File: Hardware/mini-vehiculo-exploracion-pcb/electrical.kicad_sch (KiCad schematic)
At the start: 0 parts

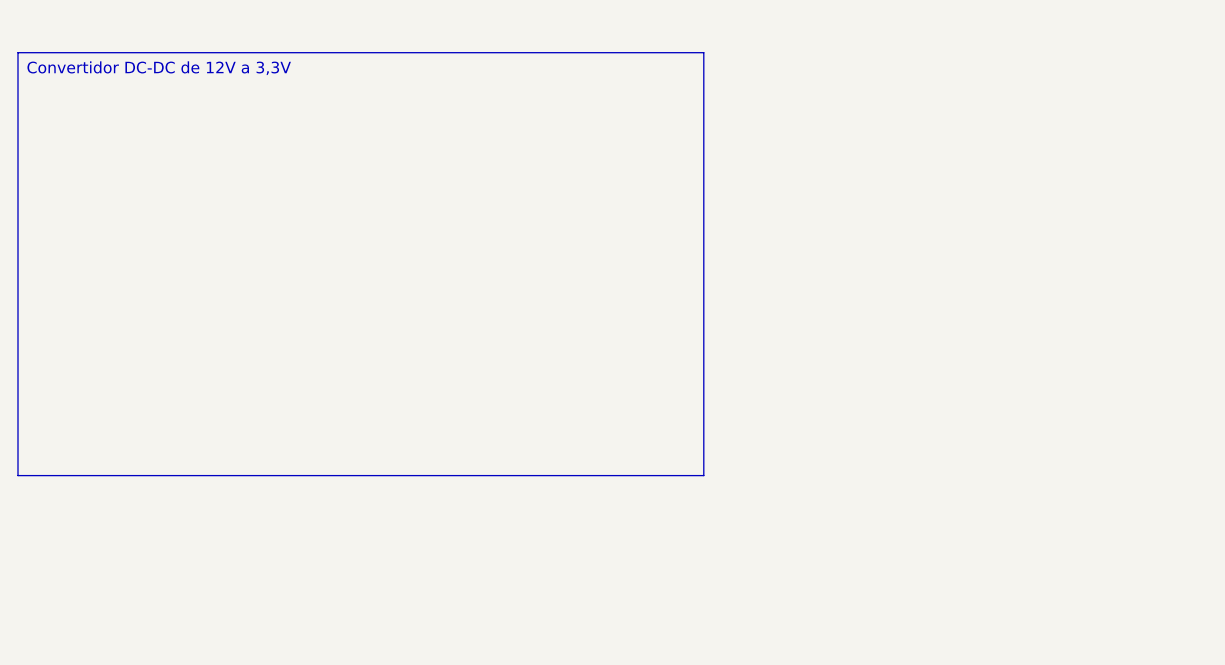
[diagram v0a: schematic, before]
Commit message: implementacion buck 3,3V
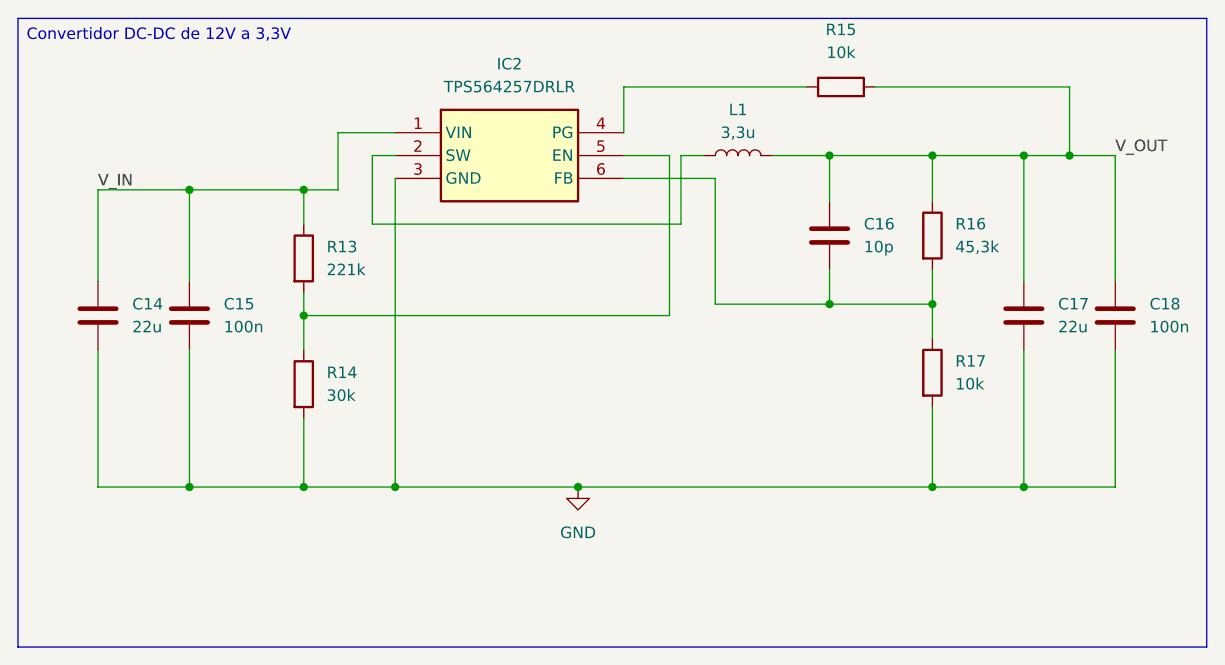
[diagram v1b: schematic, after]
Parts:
- added C14, C17: 22u, symbol Device:C
- added C15, C18: 100n, symbol Device:C
- added C16: 10p, symbol Device:C
- added IC2: TPS564257DRLR, SOTFL50P160X60-6N, symbol SamacSys_Parts:TPS564257DRLR
- added L1: 3,3u, symbol Device:L
- added R13: 221k, symbol Device:R
- added R14: 30k, symbol Device:R
- added R15, R17: 10k, symbol Device:R
- added R16: 45,3k, symbol Device:R
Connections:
- new net: C16.2, IC2.6 (FB), R16.2, R17.1
- new net: IC2.2 (SW), L1.1
- new net: IC2.5 (EN), R13.2, R14.1
- new net: IC2.4 (PG), R15.1
- new net GND: C14.2, C15.2, C17.2, C18.2, IC2.3 (GND), R14.2, R17.2
- new net V_IN: C14.1, C15.1, IC2.1 (VIN), R13.1
- new net V_OUT: C16.1, C17.1, C18.1, L1.2, R15.2, R16.1

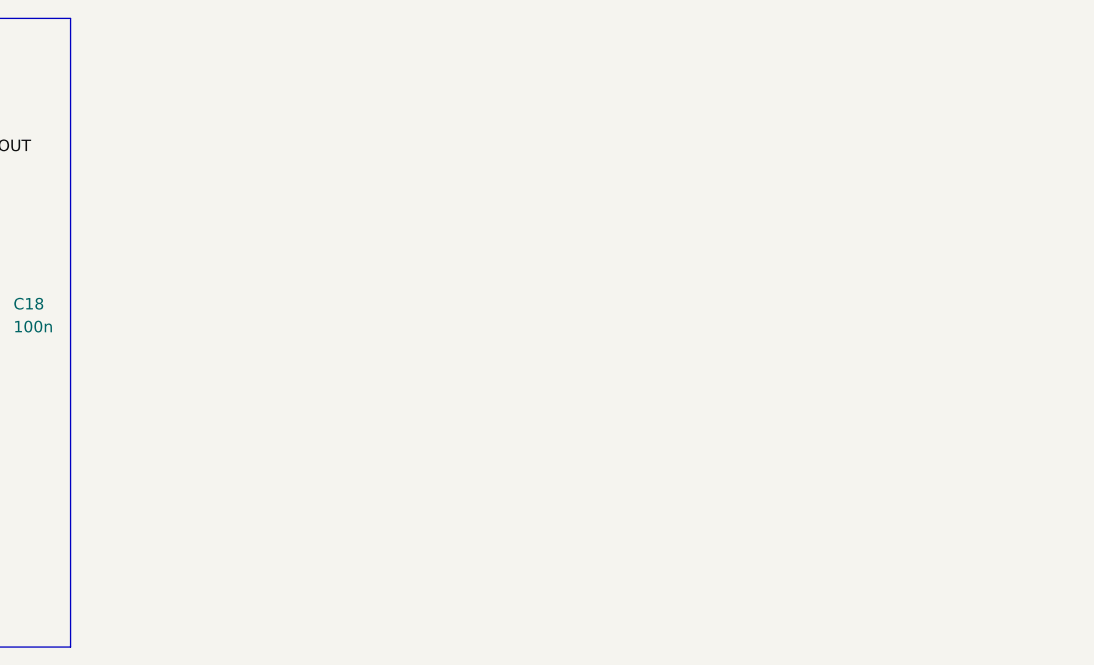
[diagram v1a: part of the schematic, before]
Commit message: LDO 5V a 3,3V
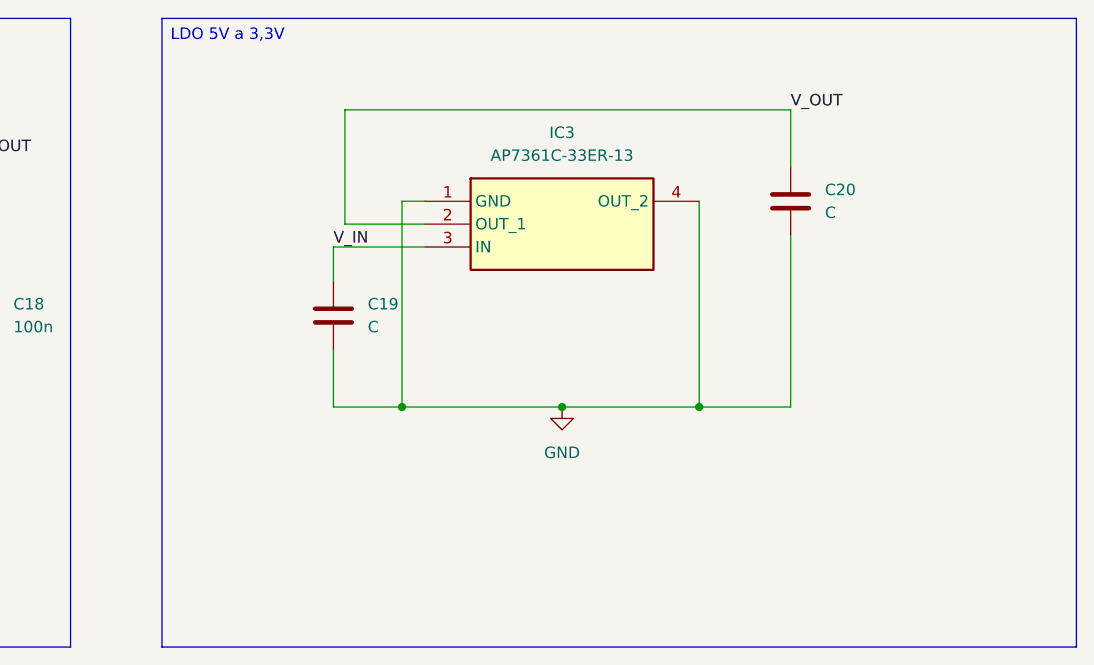
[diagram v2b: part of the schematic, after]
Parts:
- added C19, C20: C, symbol Device:C
- added IC3: AP7361C-33ER-13, SOT230P700X180-4N, symbol SamacSys_Parts:AP7361C-33ER-13
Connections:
- net GND: now also C19.2, C20.2, IC3.1 (GND), IC3.4 (OUT_2)
- net V_IN: now also C19.1, IC3.3 (IN)
- net V_OUT: now also C20.1, IC3.2 (OUT_1)

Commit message: Carga de librerias
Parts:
- added C21: 47nF, symbol Device:C
- added D3: PTVS13VP1UTP-QX, SODFL4725X110N, symbol PTVS13VP1UTP-QX:PTVS13VP1UTP-QX
- added F2: SMD200F_24-2920-2, SMD200F2429202, symbol SMD200F_24-2920-2:SMD200F_24-2920-2
- added IC4: NCV68061SNAIT1G, SOT95P275X110-6N, symbol NCV68061SNAIT1G:NCV68061SNAIT1G
- added Q1: NVMFS5C442NLAFT1G-YE, NVMFS5C430NAFT1GYE, symbol NVMFS5C442NLAFT1G-YE:NVMFS5C442NLAFT1G-YE
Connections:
- net GND: now also C21.2, D3.2 (A), IC4.2 (GND), IC4.4 (D)
- new net: D3.1 (K), F2.1
- new net: F2.2, IC4.3 (EN)
- new net: C21.1, IC4.6 (S)

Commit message: edicion parcial proteccion entrada
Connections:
- net at Q1.4 (G): now also IC4.5 (G)
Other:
- moved on the sheet: Q1
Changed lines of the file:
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@@
+	(wire
+		(pts
+			(xy 90.17 118.11) (xy 93.98 118.11)
+		)
+		(stroke
+			(width 0)
+			(type default)
+		)
+	)
 	(wire
 		(pts
@@
 	(wire
 		(pts
+			(xy 93.98 118.11) (xy 93.98 133.35)
+		)
+		(stroke
+			(width 0)
+			(type default)
+		)
+	)
+	(wire
+		(pts
 			(xy 67.31 118.11) (xy 64.77 118.11)
 		)
@@
 		(pts
 			(xy 91.44 27.94) (xy 91.44 33.02)
+		)
+		(stroke
+			(width 0)
+			(type default)
+		)
+	)
+	(wire
+		(pts
+			(xy 93.98 133.35) (xy 95.25 133.35)
 		)
 		(stroke
@@
 	(symbol
 		(lib_id "NVMFS5C442NLAFT1G-YE:NVMFS5C442NLAFT1G-YE")
-		(at 96.52 149.86 0)
+		(at 95.25 125.73 0)
 		(unit 1)
 		(exclude_from_sim no)
@@
 		(fields_autoplaced yes)
 		(property "Reference" "Q1"
-			(at 109.22 142.24 0)
+			(at 107.95 118.11 0)
 			(effects
 				(font
@@
 		)
 		(property "Value" "NVMFS5C442NLAFT1G-YE"
-			(at 109.22 144.78 0)
+			(at 107.95 120.65 0)
 			(effects
 				(font
@@
 		)
 		(property "Footprint" "NVMFS5C430NAFT1GYE"
-			(at 118.11 244.78 0)
+			(at 116.84 220.65 0)
 			(effects
 				(font
@@
 		)
 		(property "Datasheet" "https://www.onsemi.com/pub/Collateral/NVMFS5C442NL-D.PDF"
-			(at 118.11 344.78 0)
+			(at 116.84 320.65 0)
 			(effects
 				(font
@@
 		)
 		(property "Description" "Small Footprint (5x6 mm); Low RDS(on); AECQ101 Qualified and PPAP Capable; NVMFS5C442NLWF  Wettable Flank Option; Low QG and Capacitance; RoHS Compliant"
-			(at 96.52 149.86 0)
+			(at 95.25 125.73 0)
 			(effects
 				(font
@@
 		)
 		(property "Height" "1.1"
-			(at 118.11 544.78 0)
+			(at 116.84 520.65 0)
 			(effects
 				(font
@@
 		)
 		(property "Mouser Part Number" ""
-			(at 118.11 644.78 0)
+			(at 116.84 620.65 0)
 			(effects
 				(font
@@
 		)
 		(property "Mouser Price/Stock" ""
-			(at 118.11 744.78 0)
+			(at 116.84 720.65 0)
 			(effects
 				(font
@@
 		)
 		(property "Manufacturer_Name" "onsemi"
-			(at 118.11 844.78 0)
+			(at 116.84 820.65 0)
 			(effects
 				(font
@@
 		)
 		(property "Manufacturer_Part_Number" "NVMFS5C442NLAFT1G-YE"
-			(at 118.11 944.78 0)
-			(effects
-				(font
+			(at 116.84 920.65 0)
+			(effects
+				(font

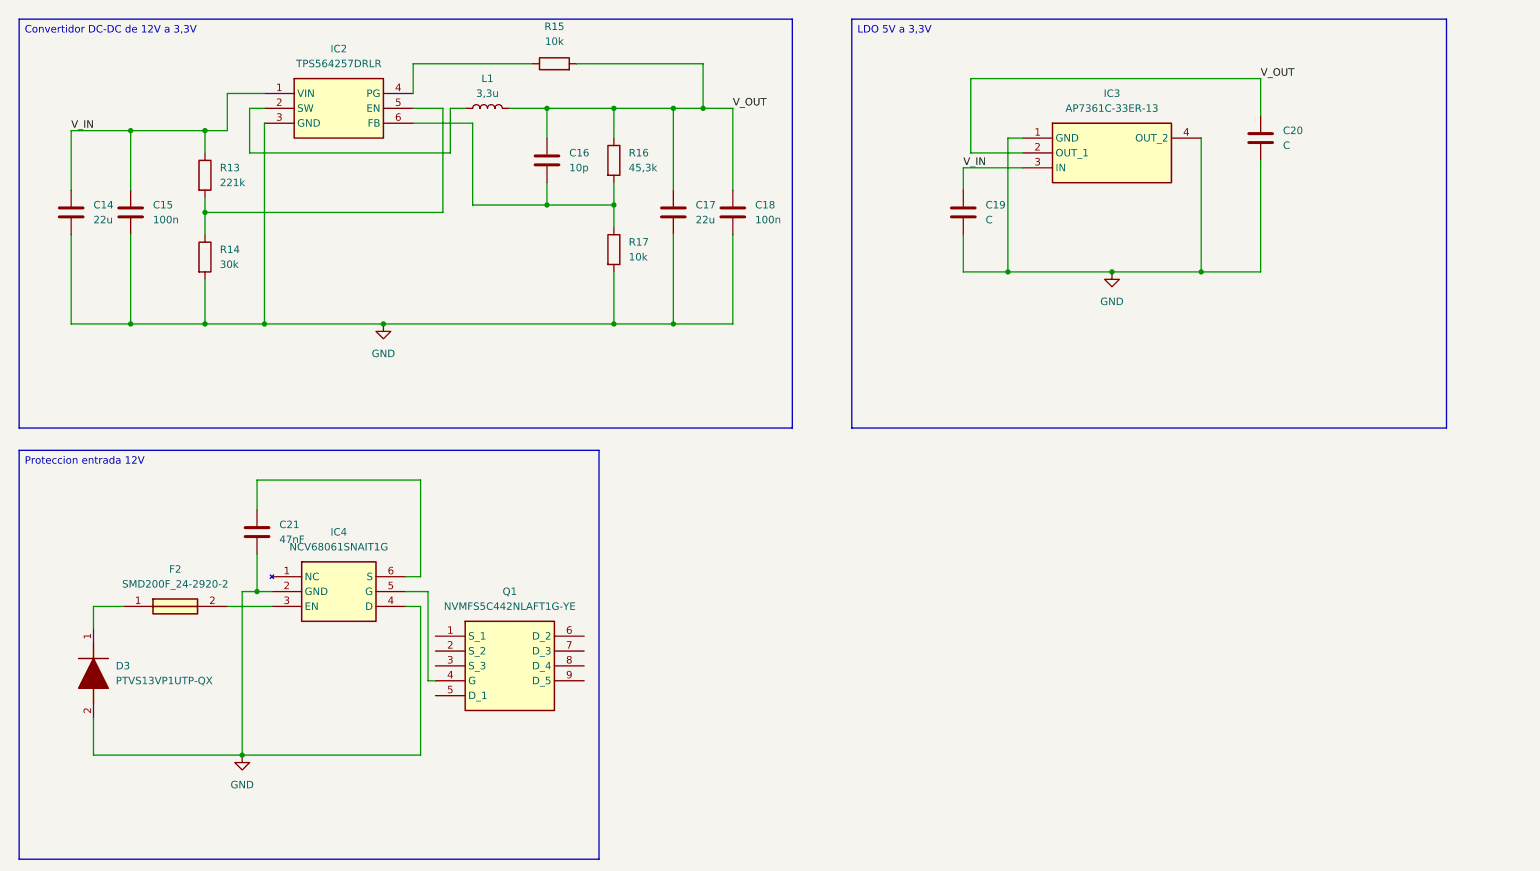
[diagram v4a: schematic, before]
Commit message: cambio de componentes e implementacion circuito de seleccion
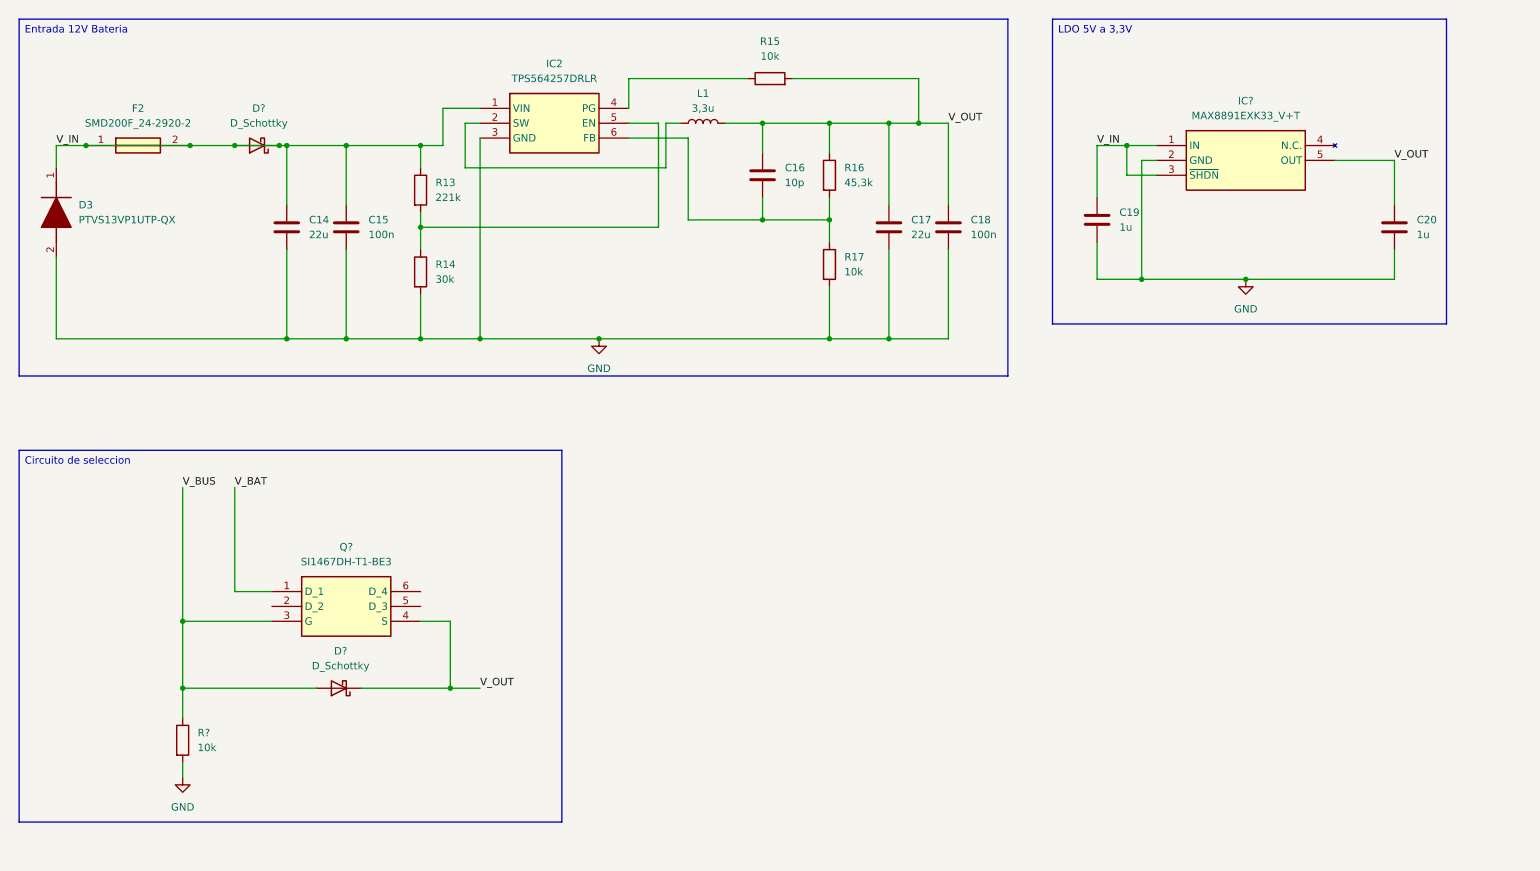
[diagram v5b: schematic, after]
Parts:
- removed C21: 47nF, symbol Device:C
- removed IC3: AP7361C-33ER-13, SOT230P700X180-4N, symbol SamacSys_Parts:AP7361C-33ER-13
- removed IC4: NCV68061SNAIT1G, SOT95P275X110-6N, symbol NCV68061SNAIT1G:NCV68061SNAIT1G
- removed Q1: NVMFS5C442NLAFT1G-YE, NVMFS5C430NAFT1GYE, symbol NVMFS5C442NLAFT1G-YE:NVMFS5C442NLAFT1G-YE
- added D? (x2): D_Schottky, symbol Device:D_Schottky
- added IC?: MAX8891EXK33_V+T, SOT65P210X110-5N, symbol MAX8891EXK33_V+T:MAX8891EXK33_V+T
- added Q?: SI1467DH-T1-BE3, SOT65P210X110-6N, symbol SI1467DH-T1-BE3:SI1467DH-T1-BE3
- added R?: 10k, symbol Device:R
- C19, C20: value C -> 1u
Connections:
- net GND: now also IC?.2 (GND), R?.2
- net V_IN: now also D3.1 (K), F2.1, F2.2, D?.1 (K), D?.2 (A), IC?.1 (IN), IC?.3 (~{SHDN})
- net V_OUT: now also D?.1 (K), IC?.5 (OUT), Q?.4 (S)
- new net V_BAT: Q?.1 (D_1)
- new net V_BUS: D?.2 (A), Q?.3 (G), R?.1
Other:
- moved on the sheet: C14, C15, C16, C17, C18, C19, C20, D3, F2, IC2, L1, R13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

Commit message: cambios
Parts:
- removed D?: D_Schottky, symbol Device:D_Schottky
- added D4: PMEG040V030EPE-QZ, PMEG040V030EPEQZ, symbol PMEG040V030EPE-QZ:PMEG040V030EPE-QZ
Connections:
- net V_IN: now also D4.1 (A_1), D4.2 (A_2); no longer C14.1, C15.1, IC2.1 (VIN), R13.1
- new net: C14.1, C15.1, D4.3 (K), IC2.1 (VIN), R13.1
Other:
- moved on the sheet: C14, C15, C16, C17, C18, IC2, L1, R13, R14, R15, R16, R17
